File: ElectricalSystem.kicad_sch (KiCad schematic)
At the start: 15 parts, among them K1 HV+ Contactor, K2 HV- Contactor, K3 Array Main Contactor, K4 Array Precharge Contactor, K5 Motor Precharge Contactor, K6 Motor Contactor, M1 Mitsuba M2096-III Motor, SW3 Supp_Enable

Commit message: done except telemetry
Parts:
- added F2: 3A?, symbol Device:Fuse
- added R3: ???, symbol Device:R
- K6: value Motor Contactor -> Motor Main Contactor
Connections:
- net ARR_HV+: now also K3.L1
- net ArrayPreRes-: now also K5.L2, F2.2, R3.2
- net HV-: now also K2.L1
- net MTR_HV+: now also K6.L1
- net MotorPreRes+: now reaches K5.L1
- net MotorPreRes+: now also K6.L2, R3.1
- new net DC-DC-Converter/HV+: F2.1
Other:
- sheet VehicleControlUnit ports: added MotorPreReady, MotorPreSPI; removed none
- note added: "add dynamics + linpot (4x), environment (6x??), TPMS transceiver (4x), broker?"
- note added: "add e-stops"
- note removed: "add bus bar connections, e-stops"
- note removed: "add fuse - bus bar?"
- note removed: "add leader (+ wireless stuff), dynamics + linpot (4x), environment (6x??), TPMS transceiver (4x), broker?"
- note removed: "bus bar?"
- note removed: "change to separate precharge boards for BPS/VCU"
- moved on the sheet: F1, R1, R2

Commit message: steering
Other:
- sheet Steering_Board ports: added +12V_PCAN, +PCAN, -PCAN, Cruise_Set, GND_PCAN, Horn, Regen, Regen_EN, Turn_Signal; removed none
- note added: "why two regen? also how do turn signals/horn interface?"

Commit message: add telemetry
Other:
- added sheet Dynamics_Board (4x) (Dynamics_Board.kicad_sch)
- added sheet Environment_Board (6x) (Environment_Board.kicad_sch)
- added sheet PeripheralSOM12 (PeripheralSOM.kicad_sch)
- added sheet PeripheralSOM13 (PeripheralSOM.kicad_sch)
- added sheet TPMS_Sensor (4x) (TPMS_Sensor.kicad_sch)
- note added: "- Controls Daughter Board - Array Blackbody sensors - Explain purpose of each CAN - Diagram CAN loop topology"
- note added: "how is TPMS implemented?"
- note added: "tentatively Meanwell RSD-300-12D may switch to smaller profile"
- note added: "terminating ends, all nodes in order"
- note removed: "- Controls Daughter Board - Steering board - Battery boards (internal HV?) - Telemetry sensors/leader - Array (MPPTs, Blackbody sensors) - Explain purpose of each CAN - Diagram CAN loop topology"
- note removed: "add dynamics + linpot (4x), environment (6x??), TPMS transceiver (4x), broker?"

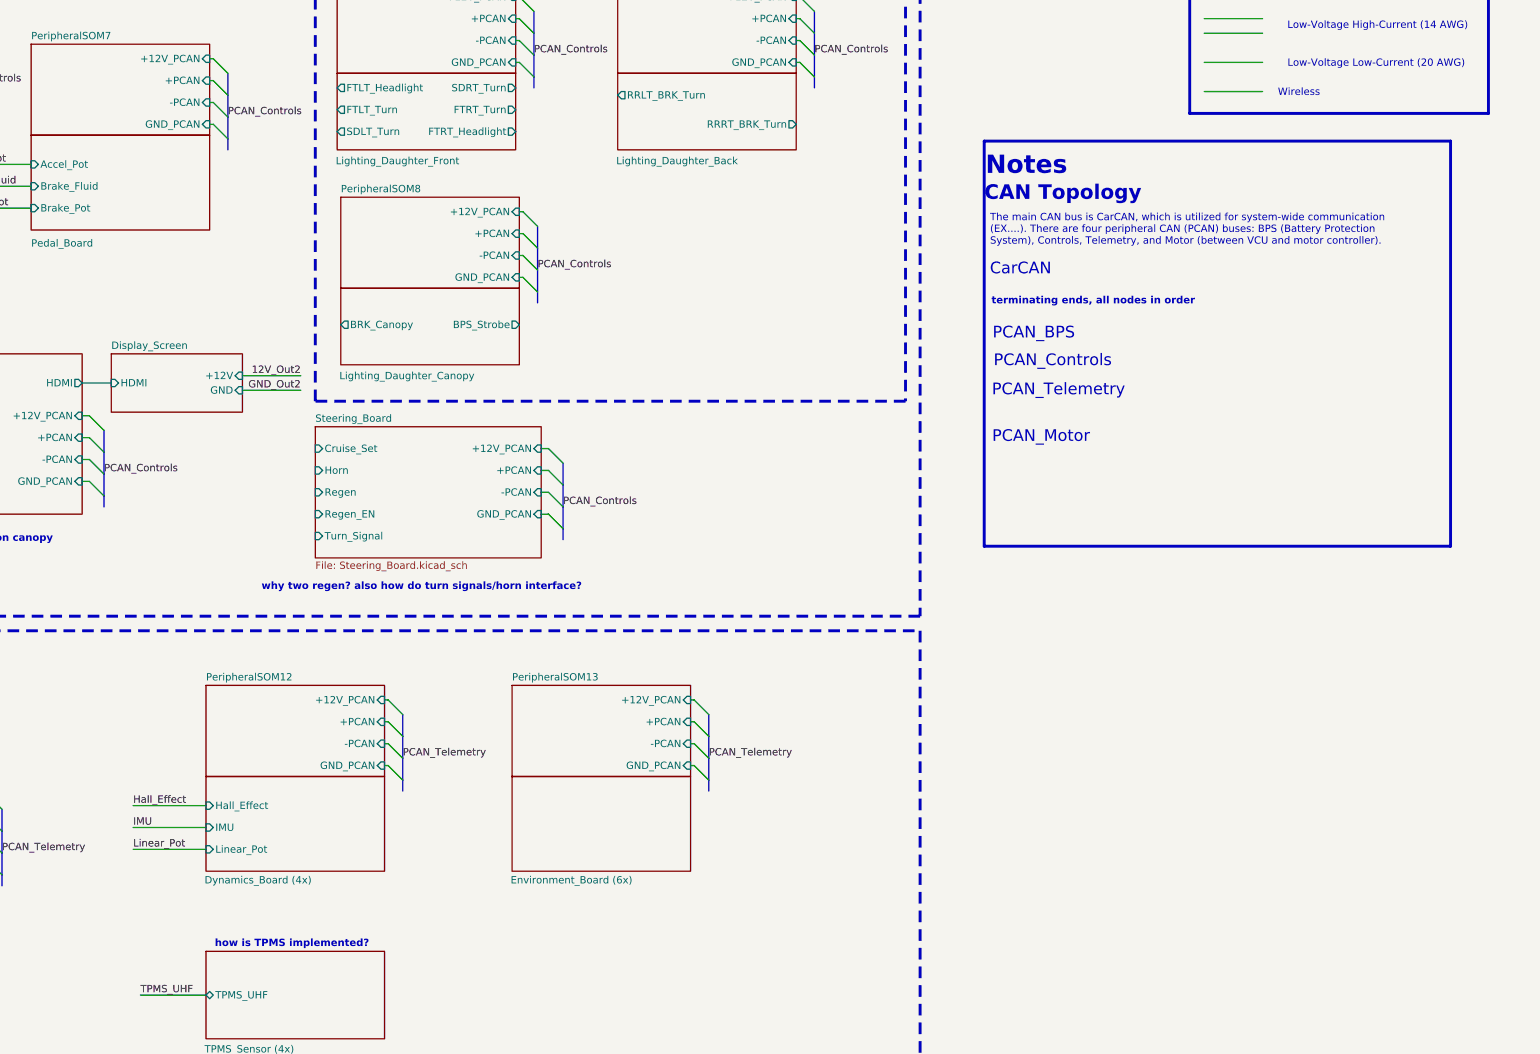
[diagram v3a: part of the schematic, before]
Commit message: can topology
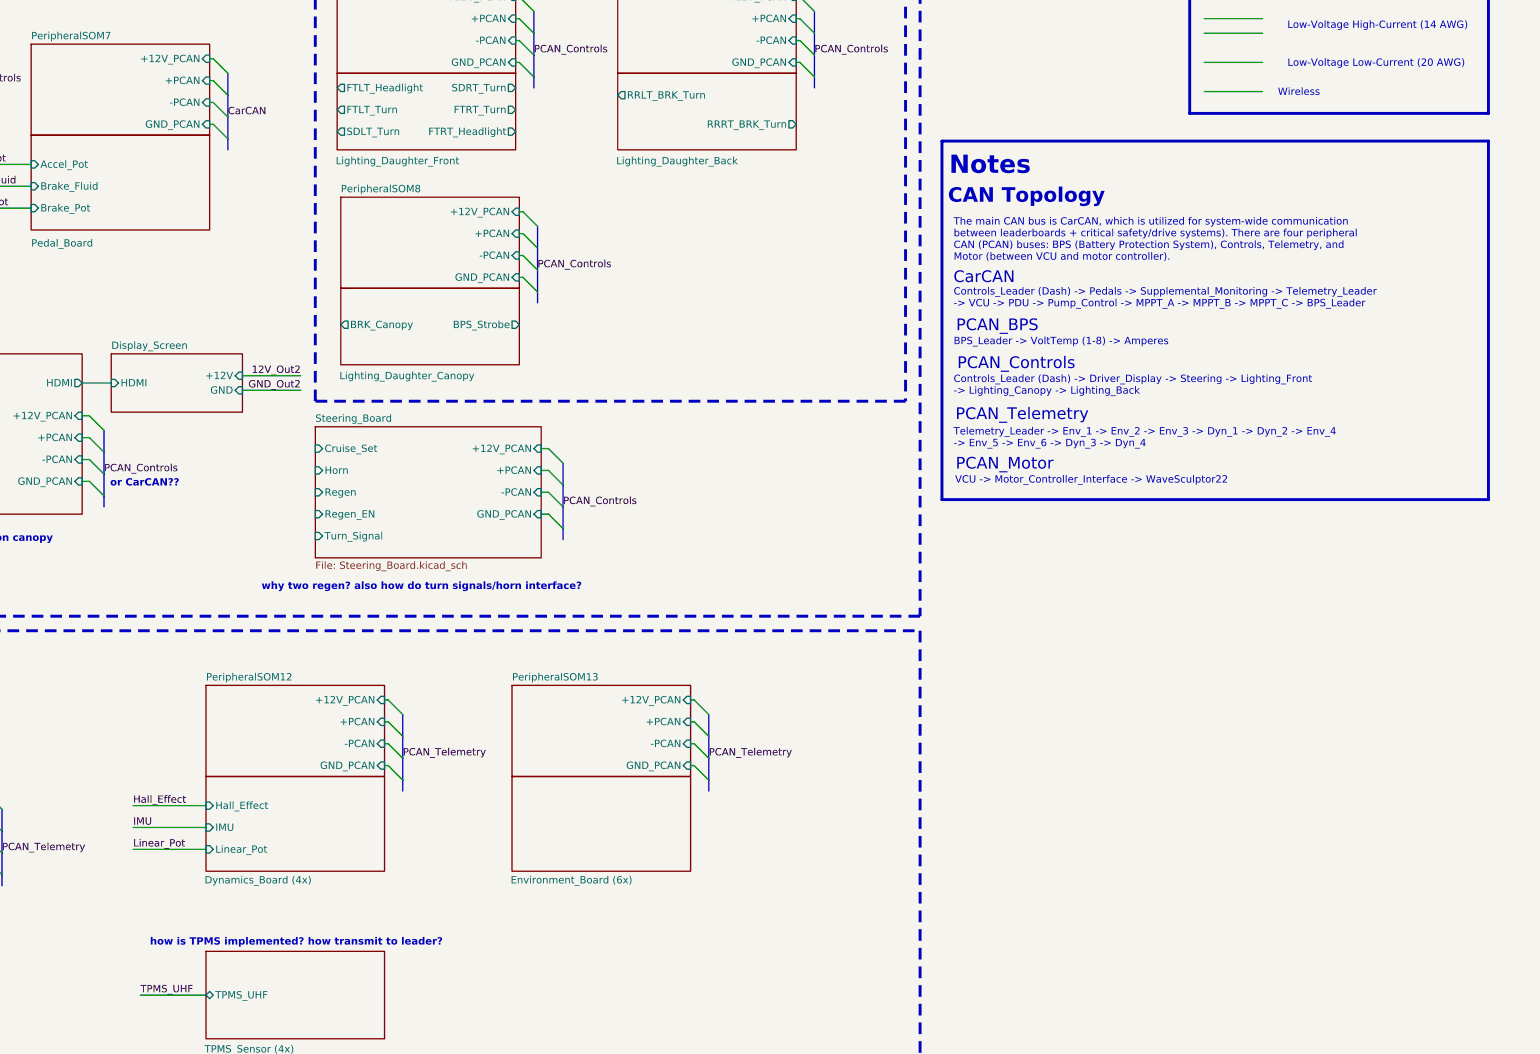
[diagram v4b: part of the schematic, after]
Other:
- note added: "BPS_Leader -> VoltTemp (1-8) -> Amperes"
- note added: "Controls_Leader (Dash) -> Driver_Display -> Steering -> Lighting_Front -> Lighting_Canopy -> Lighting_Back"
- note added: "Controls_Leader (Dash) -> Pedals -> Supplemental_Monitoring -> Telemetry_Leader -> VCU -> PDU -> Pump_Control -> MPPT_A -> MPPT_B -> MPPT_C -> BPS_Leader"
- note added: "Telemetry_Leader -> Env_1 -> Env_2 -> Env_3 -> Dyn_1 -> Dyn_2 -> Env_4 -> Env_5 -> Env_6 -> Dyn_3 -> Dyn_4"
- note added: "The main CAN bus is CarCAN, which is utilized for system-wide communication between leaderboards + critical safety/drive systems). There are four peripheral CAN (PCAN) buses: BPS (Battery Protection System), Controls, Telemetry, and Motor (between VCU and motor controller)."
- note added: "VCU -> Motor_Controller_Interface -> WaveSculptor22"
- note added: "how is TPMS implemented? how transmit to leader?"
- note added: "or CarCAN??"
- note removed: "The main CAN bus is CarCAN, which is utilized for system-wide communication (EX....). There are four peripheral CAN (PCAN) buses: BPS (Battery Protection System), Controls, Telemetry, and Motor (between VCU and motor controller)."
- note removed: "how is TPMS implemented?"
- note removed: "terminating ends, all nodes in order"
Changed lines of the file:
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@@
 	)
 	(rectangle
-		(start 657.606 61.976)
-		(end 738.886 132.588)
+		(start 650.24 61.976)
+		(end 745.49 124.46)
 		(stroke
 			(width 0.508)
@@
 		)
 	)
-	(text "The main CAN bus is CarCAN, which is utilized for system-wide communication\n(EX....). There are four peripheral CAN (PCAN) buses: BPS (Battery Protection\nSystem), Controls, Telemetry, and Motor (between VCU and motor controller)."
+	(text "The main CAN bus is CarCAN, which is utilized for system-wide communication\nbetween leaderboards + critical safety/drive systems). There are four peripheral\nCAN (PCAN) buses: BPS (Battery Protection System), Controls, Telemetry, and\nMotor (between VCU and motor controller)."
 		(exclude_from_sim no)
-		(at 658.622 77.47 0)
+		(at 652.272 79.248 0)
 		(effects
 			(font
@@
 		)
 	)
+	(text "Telemetry_Leader -> Env_1 -> Env_2 -> Env_3 -> Dyn_1 -> Dyn_2 -> Env_4\n-> Env_5 -> Env_6 -> Dyn_3 -> Dyn_4"
+		(exclude_from_sim no)
+		(at 652.272 113.792 0)
+		(effects
+			(font
+				(size 1.27 1.27)
+				(color 0 132 0 1)
+			)
+			(justify left)
+		)
+	)
 	(text "rating?"
 		(exclude_from_sim no)
@@
 		)
 	)
+	(text "BPS_Leader -> VoltTemp (1-8) -> Amperes"
+		(exclude_from_sim no)
+		(at 652.272 97.028 0)
+		(effects
+			(font
+				(size 1.27 1.27)
+				(color 132 0 132 1)
+			)
+			(justify left)
+		)
+	)
 	(text "value?"
 		(exclude_from_sim no)
@@
 	(text "CAN Topology"
 		(exclude_from_sim no)
-		(at 671.322 71.12 0)
+		(at 664.972 71.628 0)
 		(effects
 			(font
@@
 	(text "PCAN_Motor"
 		(exclude_from_sim no)
-		(at 667.512 113.538 0)
+		(at 661.162 118.364 0)
 		(effects
 			(font
 				(size 2.032 2.032)
 				(thickness 0.254)
-				(color 0 0 0 1)
+				(color 204 102 0 1)
 			)
 		)
 	)
+	(text "VCU -> Motor_Controller_Interface -> WaveSculptor22"
+		(exclude_from_sim no)
+		(at 652.526 121.158 0)
+		(effects
+			(font
+				(size 1.27 1.27)
+				(color 204 102 0 1)
+			)
+			(justify left)
+		)
+	)
 	(text "Each MPPT internally fused to 8A"
 		(exclude_from_sim no)
@@
 	(text "Notes"
 		(exclude_from_sim no)
-		(at 664.972 66.294 0)
+		(at 658.622 66.294 0)
 		(effects
 			(font
@@
 	(text "PCAN_Controls"
 		(exclude_from_sim no)
-		(at 669.544 100.33 0)
+		(at 663.194 100.838 0)
 		(effects
 			(font
 				(size 2.032 2.032)
 				(thickness 0.254)
-				(color 0 0 0 1)
+				(color 0 0 255 1)
 			)
 		)
@@
 	(text "PCAN_BPS"
 		(exclude_from_sim no)
-		(at 666.242 95.504 0)
+		(at 659.892 94.234 0)
 		(effects
 			(font
 				(size 2.032 2.032)
 				(thickness 0.254)
-				(color 0 0 0 1)
+				(color 132 0 132 1)
 			)
 		)
@@
 		)
 	)
-	(text "how is TPMS implemented?"
+	(text "or CarCAN??"
 		(exclude_from_sim no)
-		(at 536.956 201.93 0)
+		(at 511.302 121.666 0)
 		(effects
 			(font
@@
 		)
 	)
-	(text "Radiator Fans"
+	(text "how is TPMS implemented? how transmit to leader?"
 		(exclude_from_sim no)
-		(at 382.778 215.646 0)
+		(at 537.718 201.676 0)
 		(effects
 			(font
-				(size 1.016 1.016)
-				(thickness 0.127)
-				(color 0 3 255 1)
+				(size 1.27 1.27)
+				(thickness 0.254)
+				(bold yes)
+				(color 254 0 0 1)
 			)
 		)
 	)
-	(text "terminating ends, all nodes in order"
+	(text "Radiator Fans"
 		(exclude_from_sim no)
-		(at 658.876 89.916 0)
+		(at 382.778 215.646 0)
 		(effects
 			(font
-				(size 1.27 1.27)
-				(thickness 0.254)
-				(bold yes)
-				(color 255 0 0 1)
+				(size 1.016 1.016)
+				(thickness 0.127)
+				(color 0 3 255 1)
 			)
-			(justify left)
 		)
 	)
@@
 	(text "PCAN_Telemetry"
 		(exclude_from_sim no)
-		(at 670.56 105.41 0)
+		(at 664.21 109.728 0)
 		(effects
 			(font
 				(size 2.032 2.032)
 				(thickness 0.254)
-				(color 0 0 0 1)
+				(color 0 132 0 1)
 			)
 		)
 	)
+	(text "Controls_Leader (Dash) -> Driver_Display -> Steering -> Lighting_Front\n-> Lighting_Canopy -> Lighting_Back"
+		(exclude_from_sim no)
+		(at 652.272 104.648 0)
+		(effects
+			(font
+				(size 1.27 1.27)
+				(color 0 0 255 1)
+			)
+			(justify left)
+		)
+	)
 	(text "Array"
 		(exclude_from_sim no)
@@
 	(text "CarCAN"
 		(exclude_from_sim no)
-		(at 663.956 84.328 0)
+		(at 657.606 85.852 0)
 		(effects
 			(font
@@
 		)
 	)
+	(text "Controls_Leader (Dash) -> Pedals -> Supplemental_Monitoring -> Telemetry_Leader\n-> VCU -> PDU -> Pump_Control -> MPPT_A -> MPPT_B -> MPPT_C -> BPS_Leader"
+		(exclude_from_sim no)
+		(at 652.272 89.408 0)
+		(effects
+			(font
+				(size 1.27 1.27)
+				(color 0 0 0 1)
+			)
+			(justify left)
+		)
+	)
 	(text "Determine what dashboard LEDs and buttons will be connected"
 		(exclude_from_sim no)
@@
 		)
 	)
-	(label "PCAN_Controls"
+	(label "CarCAN"
 		(at 525.78 57.785 0)
 		(effects

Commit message: add suppmon shunt
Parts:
- added R4: ???, symbol Device:R_Shunt
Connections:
- net PowerBoard/GND_Supp: now also R4.4
- new net Supp_Shunt+: R4.3
- new net Supp_Shunt-: R4.2
- new net SupplementalBattery/GND_Supp: R4.1
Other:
- sheet SuppMonitoringBoard ports: added Shunt+, Shunt-; removed none
- note added: "- Controls Daughter Board - Array Blackbody sensors"
- note removed: "- Controls Daughter Board - Array Blackbody sensors - Explain purpose of each CAN - Diagram CAN loop topology"
- note removed: "add shunt?"
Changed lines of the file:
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@@
 	(rectangle
 		(start 649.732 16.51)
-		(end 688.848 31.75)
+		(end 688.848 57.15)
 		(stroke
 			(width 0.508)
@@
 		)
 	)
+	(text "value?"
+		(exclude_from_sim no)
+		(at 358.14 270.002 0)
+		(effects
+			(font
+				(size 1.27 1.27)
+				(thickness 0.254)
+				(bold yes)
+				(color 255 0 0 1)
+			)
+		)
+	)
 	(text "PCAN_Controls"
 		(exclude_from_sim no)
@@
 		)
 	)
-	(text "- Controls Daughter Board\n- Array Blackbody sensors\n- Explain purpose of each CAN\n- Diagram CAN loop topology"
+	(text "- Controls Daughter Board\n- Array Blackbody sensors"
 		(exclude_from_sim no)
-		(at 651.51 25.654 0)
+		(at 651.51 23.114 0)
 		(effects
 			(font
@@
 		)
 	)
-	(text "add shunt?"
-		(exclude_from_sim no)
-		(at 378.46 319.278 0)
-		(effects
-			(font
-				(size 1.27 1.27)
-				(thickness 0.254)
-				(bold yes)
-				(color 255 0 0 1)
-			)
-		)
-	)
 	(text "TODO:\n"
 		(exclude_from_sim no)
@@
 	)
 	(junction
-		(at 335.28 267.97)
+		(at 339.09 267.97)
 		(diameter 0)
 		(color 0 0 0 0)
@@
 		)
 	)
+	(wire
+		(pts
+			(xy 354.33 271.78) (xy 354.33 285.75)
+		)
+		(stroke
+			(width 0)
+			(type default)
+		)
+	)
 	(bus
 		(pts
@@
 	(wire
 		(pts
-			(xy 342.9 300.99) (xy 361.95 300.99)
+			(xy 342.9 299.72) (xy 361.95 299.72)
 		)
 		(stroke
@@
 	(wire
 		(pts
-			(xy 342.9 264.16) (xy 342.9 300.99)
+			(xy 342.9 264.16) (xy 342.9 299.72)
 		)
 		(stroke
@@
 	(wire
 		(pts
-			(xy 270.51 267.97) (xy 335.28 267.97)
+			(xy 270.51 267.97) (xy 339.09 267.97)
 		)
 		(stroke
@@
 	(wire
 		(pts
-			(xy 335.28 308.61) (xy 361.95 308.61)
+			(xy 339.09 303.53) (xy 361.95 303.53)
 		)
 		(stroke
@@
 		)
 	)
+	(wire
+		(pts
+			(xy 339.09 267.97) (xy 346.71 267.97)
+		)
+		(stroke
+			(width 0)
+			(type default)
+			(color 72 72 72 1)
+		)
+	)
 	(bus
 		(pts
@@
 	(wire
 		(pts
+			(xy 356.87 267.97) (xy 361.95 267.97)
+		)
+		(stroke
+			(width 0)
+			(type default)
+			(color 72 72 72 1)
+		)
+	)
+	(wire
+		(pts
 			(xy 156.21 110.49) (xy 158.75 110.49)
 		)
@@
 	(wire
 		(pts
+			(xy 349.25 271.78) (xy 349.25 285.75)
+		)
+		(stroke
+			(width 0)
+			(type default)
+		)
+	)
+	(wire
+		(pts
 			(xy 251.46 114.3) (xy 264.16 114.3)
 		)
@@
 	(wire
 		(pts
-			(xy 335.28 267.97) (xy 335.28 308.61)
+			(xy 339.09 267.97) (xy 339.09 303.53)
 		)
 		(stroke
@@
 	(wire
 		(pts
+			(xy 347.98 307.34) (xy 361.95 307.34)
+		)
+		(stroke
+			(width 0)
+			(type default)
+		)
+	)
+	(wire
+		(pts
 			(xy 315.595 60.325) (xy 323.85 60.325)
 		)
@@
 	(wire
 		(pts
+			(xy 347.98 311.15) (xy 361.95 311.15)
+		)
+		(stroke
+			(width 0)
+			(type default)
+		)
+	)
+	(wire
+		(pts
 			(xy 474.98 297.18) (xy 481.33 297.18)
 		)
@@
 	(wire
 		(pts
-			(xy 335.28 267.97) (xy 361.95 267.97)
-		)
-		(stroke
-			(width 0)
-			(type default)
-			(color 72 72 72 1)
-		)
-	)
-	(wire
-		(pts
 			(xy 360.68 209.55) (xy 370.84 209.55)
 		)
@@
 		)
 	)
+	(label "Supp_Shunt-"
+		(at 347.98 311.15 0)
+		(effects
+			(font
+				(size 1.27 1.27)
+			)
+			(justify left bottom)
+		)
+	)
 	(label "GND_ARR"
 		(at 261.62 50.8 180)
@@
 		)
 	)
+	(label "Supp_Shunt+"
+		(at 347.98 307.34 0)
+		(effects
+			(font
+				(size 1.27 1.27)
+			)
+			(justify left bottom)
+		)
+	)
 	(label "Temp4"
 		(at 304.165 149.225 180)
@@
 		)
 	)
+	(label "Supp_Shunt+"
+		(at 349.25 285.75 90)
+		(effects
+			(font
+				(size 1.27 1.27)
+			)
+			(justify left bottom)
+		)
+	)
 	(label "Temp5"
 		(at 304.165 151.765 180)
@@
 		)
 	)
+	(label "Supp_Shunt-"
+		(at 354.33 285.75 90)
+		(effects
+			(font
+				(size 1.27 1.27)
+			)
+			(justify left bottom)
+		)
+	)
 	(label "MTR_HV+"
 		(at 264.16 114.3 180)
@@
 	)
 	(symbol
+		(lib_id "Device:R_Shunt")
+		(at 351.79 267.97 270)
+		(unit 1)
+		(exclude_from_sim no)
+		(in_bom yes)
+		(on_board yes)
+		(dnp no)
+		(property "Reference" "R4"
+			(at 351.79 265.684 90)
+			(effects
+				(font
+					(size 1.27 1.27)
+				)
+			)
+		)
+		(property "Value" "???"
+			(at 351.79 267.97 90)
+			(effects
+				(font
+					(size 1.27 1.27)
+				)
+			)
+		)
+		(property "Footprint" ""
+			(at 351.79 266.192 90)
+			(effects
+				(font
+					(size 1.27 1.27)
+				)
+				(hide yes)
+			)
+		)
+		(property "Datasheet" "~"
+			(at 351.79 267.97 0)
+			(effects
+				(font
+					(size 1.27 1.27)
+				)
+				(hide yes)
+			)
+		)
+		(property "Description" "Shunt resistor"
+			(at 351.79 267.97 0)
+			(effects
+				(font
+					(size 1.27 1.27)
+				)
+				(hide yes)
+			)
+		)
+		(pin "3"
+		)
+		(pin "1"
+		)
+		(pin "2"
+		)
+		(pin "4"
+		)
+		(instances
+			(project "ElectricalSystem"
+				(path "/7dc721ab-4b7a-42e7-8fa4-f406a2ddcd46"
+					(reference "R4")
+					(unit 1)
+				)
+			)
+		)
+	)
+	(symbol
 		(lib_id "Device:Solar_Cells")
 		(at 481.33 331.47 0)
@@
 		)
 		(pin "+12V_Supp" input
-			(at 361.95 300.99 180)
+			(at 361.95 299.72 180)
 			(effects
 				(font
@@
 		)
 		(pin "GND_Supp" input
-			(at 361.95 308.61 180)
+			(at 361.95 303.53 180)
+			(effects
+				(font
+					(size 1.27 1.27)
+				)
+				(justify left)
+			)
+		)
+		(pin "Shunt+" input
+			(at 361.95 307.34 180)
+			(effects
+				(font
+					(size 1.27 1.27)
+				)
+				(justify left)
+			)
+		)
+		(pin "Shunt-" input
+			(at 361.95 311.15 180)
 			(effects
 				(font

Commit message: yuh
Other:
- note added: "add physical fuses here? rating?"
- note added: "fuse b/t array and mppt?"
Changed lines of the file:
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@@
 		)
 	)
+	(text "fuse b/t array and mppt?"
+		(exclude_from_sim no)
+		(at 497.84 278.13 0)
+		(effects
+			(font
+				(size 1.27 1.27)
+				(thickness 0.254)
+				(bold yes)
+				(color 254 0 0 1)
+			)
+		)
+	)
 	(text "Determine how many USB/whether using USB hub on canopy"
 		(exclude_from_sim no)
@@
 		)
 	)
+	(text "add physical fuses here?\nrating?"
+		(exclude_from_sim no)
+		(at 185.674 278.638 0)
+		(effects
+			(font
+				(size 1.27 1.27)
+				(thickness 0.254)
+				(bold yes)
+				(color 255 0 0 1)
+			)
+		)
+	)
 	(text "Custom Bus Bar (cross-section?)"
 		(exclude_from_sim no)
@@
 	(wire
 		(pts
-			(xy 252.73 209.55) (xy 261.62 209.55)
+			(xy 252.73 209.55) (xy 265.43 209.55)
 		)
 		(stroke
@@
 	(wire
 		(pts
-			(xy 252.73 214.63) (xy 261.62 214.63)
+			(xy 252.73 214.63) (xy 265.43 214.63)
 		)
 		(stroke
@@
 		)
 	)
-	(label "Fan2"
-		(at 261.62 214.63 180)
+	(label "MocoFan2"
+		(at 265.43 214.63 180)
 		(effects
 			(font
@@
 		)
 	)
-	(label "Fan1"
-		(at 261.62 209.55 180)
+	(label "MocoFan1"
+		(at 265.43 209.55 180)
 		(effects
 			(font

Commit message: so the car has 3 wheels....
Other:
- sheet Dynamics_Board (4x) renamed Dynamics_Board (3x)
- sheet TPMS_Sensor (4x) renamed TPMS_Sensor (3x)
- note added: "add blackbody A/C (temp/irradiance sensors) 1 C per MPPT, 2 A per C"
- note removed: "add blackbody A/C (temp/irradiance sensors)"
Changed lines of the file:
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@@
 		)
 	)
-	(text "add blackbody A/C (temp/irradiance sensors)"
+	(text "add blackbody A/C (temp/irradiance sensors)\n1 C per MPPT, 2 A per C"
 		(exclude_from_sim no)
 		(at 545.084 290.322 0)
@@
 			(color 0 0 0 0.0000)
 		)
-		(property "Sheetname" "Dynamics_Board (4x)"
+		(property "Sheetname" "Dynamics_Board (3x)"
 			(at 521.716 191.516 0)
 			(effects
@@
 			(color 0 0 0 0.0000)
 		)
-		(property "Sheetname" "TPMS_Sensor (4x)"
+		(property "Sheetname" "TPMS_Sensor (3x)"
 			(at 521.716 220.98 0)
 			(effects
